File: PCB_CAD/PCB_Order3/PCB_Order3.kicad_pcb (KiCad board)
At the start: 4 copper layers, 88 parts, among them SW1 SLW-883935-2A-D

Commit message: pinned out 3 sides of the microcontroller
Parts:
- removed RCAA1, RCAA2: FW6190, CustomModels:FW6190
- removed RCAD1, RCAD2: RCJ-027, CustomModels:CUI_RCJ-027
- added J1: Conn_01x03_Socket, Connector_PinSocket_2.54mm:PinSocket_1x03_P2.54mm_Vertical_SMD_Pin1Right, F.Cu at (154.9, 137.9)
- added MbC1: 4.7u, Capacitor_SMD:C_0805_2012Metric_Pad1.18x1.45mm_HandSolder, F.Cu at (-25.4, 41.1)
- added PEC3: 47u, Capacitor_SMD:C_0805_2012Metric_Pad1.18x1.45mm_HandSolder, F.Cu at (-25.4, 44.1)
- added RCAAin1: FW6190, CustomModels:FW6190, F.Cu at (33.3, 145.5)
- added RCAAout1: FW6190, CustomModels:FW6190, F.Cu at (63.1, 145.5)
- added RCADin1: RCJ-027, CustomModels:CUI_RCJ-027, F.Cu at (97.0, 151.6)
- added RCADout1: RCJ-027, CustomModels:CUI_RCJ-027, F.Cu at (110.9, 151.5)
- MR1, MbC2, MbC3, MbC4, UR1, UR2: moved to B.Cu
- moved DCPEM1 160.2 mm to (199.5, 70.9), turned to 90 degrees
- moved DnC1 140.1 mm to (-68.5, 28.2)
- moved DrC1 140.1 mm to (-68.5, 31.2)
- moved FnC1 140.1 mm to (-68.5, 34.3)
- moved FnC2 140.1 mm to (-68.5, 37.3)
- moved LLSIC1 140.1 mm to (-68.5, 40.3)
- moved LLSIC2 140.1 mm to (-68.5, 43.3)
- moved LLSOC1 140.1 mm to (-68.5, 46.3)
- moved LLSOC2 140.1 mm to (-68.5, 49.3)
- moved LnC1 140.1 mm to (-68.5, 52.3)
- moved MnC1 140.1 mm to (-63.7, 37.3)
- moved MnC2 140.1 mm to (-63.7, 40.3)
- moved MnC3 140.1 mm to (-63.7, 43.3)
- moved MnC4 140.1 mm to (-63.7, 46.3)
- moved MnC5 140.1 mm to (-63.7, 49.3)
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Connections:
- DCPEM1 pad 1: Net-(DCPEM1-Pad1) -> GNDD
- DCPEM1 pad 2: Net-(DCPEM1-Pad2) -> VDD
- PEC1 pad 1: Net-(DCPEM1-Pad1) -> GNDD
- PEC1 pad 2: Net-(DCPEM1-Pad2) -> VDD
- PEC2 pad 1: Net-(DCPEM1-Pad1) -> GNDD
- PEC2 pad 2: Net-(DCPEM1-Pad2) -> VDD
- SPDIFTX1 pad 10: /I2S3_SDO -> /I2S2_SDO
- SPDIFTX1 pad 7: /I2S3_MCK -> /I2S2_MCK
- SPDIFTX1 pad 8: /I2S3_CK -> /I2S2_CK
- SPDIFTX1 pad 9: /I2S3_WS -> /I2S2_WS
- TVS1 pad 1: Net-(DCPEM1-Pad2) -> VDD
- TVS1 pad 2: Net-(DCPEM1-Pad1) -> GNDD
- uController1 pad 105: unconnected-(uController1-PA13-Pad105) -> /DEBUG_SWDIO
- uController1 pad 109: unconnected-(uController1-PA14-Pad109) -> /DEBUG_SWCLK
- uController1 pad 111: /I2S3_CK -> unconnected-(uController1-PC10-Pad111)
- uController1 pad 40: /I2S3_WS -> unconnected-(uController1-PA4-Pad40)
- uController1 pad 48: /I2S3_SDO -> unconnected-(uController1-PB2-Pad48)
- uController1 pad 97: /I2S3_MCK -> unconnected-(uController1-PC7-Pad97)
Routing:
- net /FMC_D0: track 0.00 -> 231.6 mm, vias 0 -> 6
- net /FMC_D7: track 0.00 -> 182.6 mm, vias 0 -> 6
- net /FMC_D6: track 0.00 -> 181.7 mm, vias 0 -> 6
- net /FMC_D5: track 0.00 -> 179.8 mm, vias 0 -> 6
- net /FMC_SDCLK: track 0.00 -> 151.8 mm, vias 0 -> 3
- net /FMC_D15: track 0.00 -> 141.6 mm, vias 0 -> 3
- net /FMC_D14: track 0.00 -> 137.0 mm, vias 0 -> 3
- net /FMC_BA1: track 0.00 -> 134.3 mm, vias 0 -> 3
- net /FMC_D13: track 0.00 -> 133.1 mm, vias 0 -> 3
- net /FMC_BA0: track 0.00 -> 133.0 mm, vias 0 -> 3
- net /I2S1_MCK: track 0.00 -> 123.9 mm, vias 0 -> 3
- net /I2S1_CK: track 0.00 -> 122.9 mm, vias 0 -> 3
- net /I2S1_SDI: track 0.00 -> 121.5 mm, vias 0 -> 3
- net /I2S2_WS: track 0.00 -> 107.9 mm, vias 0 -> 3
- net /I2S2_CK: track 0.00 -> 107.2 mm, vias 0 -> 3
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
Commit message: finished pinning out the microcontroller
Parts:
- moved SR1 195.5 mm to (122.7, 133.9), turned to 90 degrees
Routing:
- net /FMC_D3: track 0.00 -> 211.7 mm, vias 0 -> 6
- net /FMC_D2: track 0.00 -> 211.1 mm, vias 0 -> 6
- net /I2S1_WS: track 0.00 -> 116.6 mm, vias 0 -> 3
- net /FMC_NBL0: track 0.00 -> 99.9 mm, vias 0 -> 5
- net /FMC_SDNCAS: track 0.00 -> 88.9 mm, vias 0 -> 3
- net /FMC_NWE: track 0.00 -> 81.8 mm, vias 0 -> 3
- net /SPDIFRX_IN0: track 0.00 -> 80.1 mm, vias 0 -> 3
- net /FMC_NWAIT: track 0.00 -> 78.9 mm, vias 0 -> 3
- net /FMC_NBL1: track 0.00 -> 77.0 mm, vias 0 -> 3
- net /FMC_NOE: track 0.00 -> 74.7 mm, vias 0 -> 3
- net /DEBUG_SWCLK: track 0.00 -> 71.5 mm, vias 0 -> 1
- net /BOOTSW: track 0.00 -> 47.4 mm, vias 0 -> 1
- net /I2C1_SDA: track 0.00 -> 45.9 mm, vias 0 -> 1
- net /I2C1_SCL: track 0.00 -> 45.0 mm, vias 0 -> 1
- net VDD: track 14.5 -> 30.0 mm, vias 10 -> 20
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
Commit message: complete? pcb design
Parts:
- removed LLS1, LLS2: SN74AXCH1T45DCKR, CustomModels:DCK6_TEX
- added DXnC2: 0.1u, Capacitor_SMD:C_0805_2012Metric_Pad1.18x1.45mm_HandSolder, B.Cu at (109.1, 134.9)
- added DXnC3: 0.1u, Capacitor_SMD:C_0805_2012Metric_Pad1.18x1.45mm_HandSolder, B.Cu at (111.1, 134.9)
- added LLSIN1: SN74AXCH1T45DCKR, CustomModels:DCK6_TEX, F.Cu at (97.0, 143.1)
- added LLSOUT1: SN74AXCH1T45DCKR, CustomModels:DCK6_TEX, F.Cu at (110.8, 143.2)
- AB1, AbC1, AbC2, AdbC1, AdbC2, AnC1, AnC2, DB1, DacOut_L_decouple1, DacOut_L_res1, DacOut_R_decouple1, DacOut_R_res1, Dac_DigitalSup_noise1, Dac_DigitalSup_noise2, DbC1, DnC1, DrC1, FnC1, FnC2, PEC1, PEC2, PEC3, RnC1, RnC2, RnC3, RnC4, RnC5, RnC6, RnC7, SPDIFC1, SPDIFC2, SPDIFR1, SPDIFR2, VDIVR1, VDIVR2: moved to B.Cu
- DXnC1, LLSOC1: value 0.15u -> 0.1u; moved to B.Cu
- LLSOC2: value 0.15u -> 0.1u
- TVS1: footprint CustomModels:SOD-962 SL2_TOS -> Diode_SMD:D_0201_0603Metric_Pad0.64x0.40mm_HandSolder; moved to B.Cu
- moved PEC1 286.3 mm to (176.9, 122.1), turned to -90 degrees
- moved TVS1 284.4 mm to (178.3, 122.1), turned to 90 degrees
- moved PEC2 283.5 mm to (174.9, 122.1), turned to -90 degrees
- moved FnC1 252.3 mm to (177.3, 91.0), turned to 180 degrees
- moved FnC2 249.4 mm to (177.5, 78.0), turned to 180 degrees
- moved BC1 231.2 mm to (133.2, 132.1)
- moved DXnC1 213.3 mm to (113.1, 134.9), turned to -90 degrees
- moved PEC3 213.1 mm to (172.9, 122.1), turned to 90 degrees
- moved LLSOC1 206.3 mm to (113.5, 143.3), turned to 180 degrees
- moved LLSOC2 199.8 mm to (107.5, 143.6), turned to 90 degrees
- moved LnC1 196.7 mm to (128.2, 53.4)
- moved MnC6 195.4 mm to (127.7, 91.7), turned to 90 degrees
- moved LLSIC2 195.3 mm to (101.0, 140.3), turned to 90 degrees
- moved MnC2 195.3 mm to (127.5, 80.0), turned to 90 degrees
- moved MnC4 195.2 mm to (127.5, 85.2), turned to 90 degrees
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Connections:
- SPDIFTX1 pad 36: unconnected-(SPDIFTX1-VDDRX-Pad36) -> VDD
- SPDIFTX1 pad 38: unconnected-(SPDIFTX1-GNDRX-Pad38) -> GNDD
- SPDIFTX1 pad 41: unconnected-(SPDIFTX1-AGND-Pad41) -> GNDD
- SPDIFTX1 pad 42: unconnected-(SPDIFTX1-VCC-Pad42) -> VDD
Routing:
- net GNDD: track 32.1 -> 154.1 mm, vias 16 -> 65
- net VDD: track 30.0 -> 128.7 mm, vias 20 -> 51
- net /I2S2_SDO: track 0.00 -> 91.8 mm, vias 0 -> 3
- net /I2C2_SDA: track 64.8 -> 25.1 mm
- net /I2C2_SCL: track 61.9 -> 23.8 mm
- net /KP_Col3: track 84.0 -> 47.5 mm
- net /KP_Row2: track 85.9 -> 49.6 mm
- net /KP_Row1: track 83.4 -> 47.4 mm
- net /KP_Row3: track 87.4 -> 51.5 mm
- net /KP_Col2: track 89.0 -> 53.3 mm
- net /KP_Col1: track 90.7 -> 55.4 mm
- net /KP_Row4: track 72.6 -> 37.6 mm
- net /KP_Col5: track 78.7 -> 44.2 mm
- net /KP_Col4: track 79.2 -> 44.9 mm
- net /I2S2_MCK: track 91.8 -> 115.1 mm, vias 3 -> 5
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
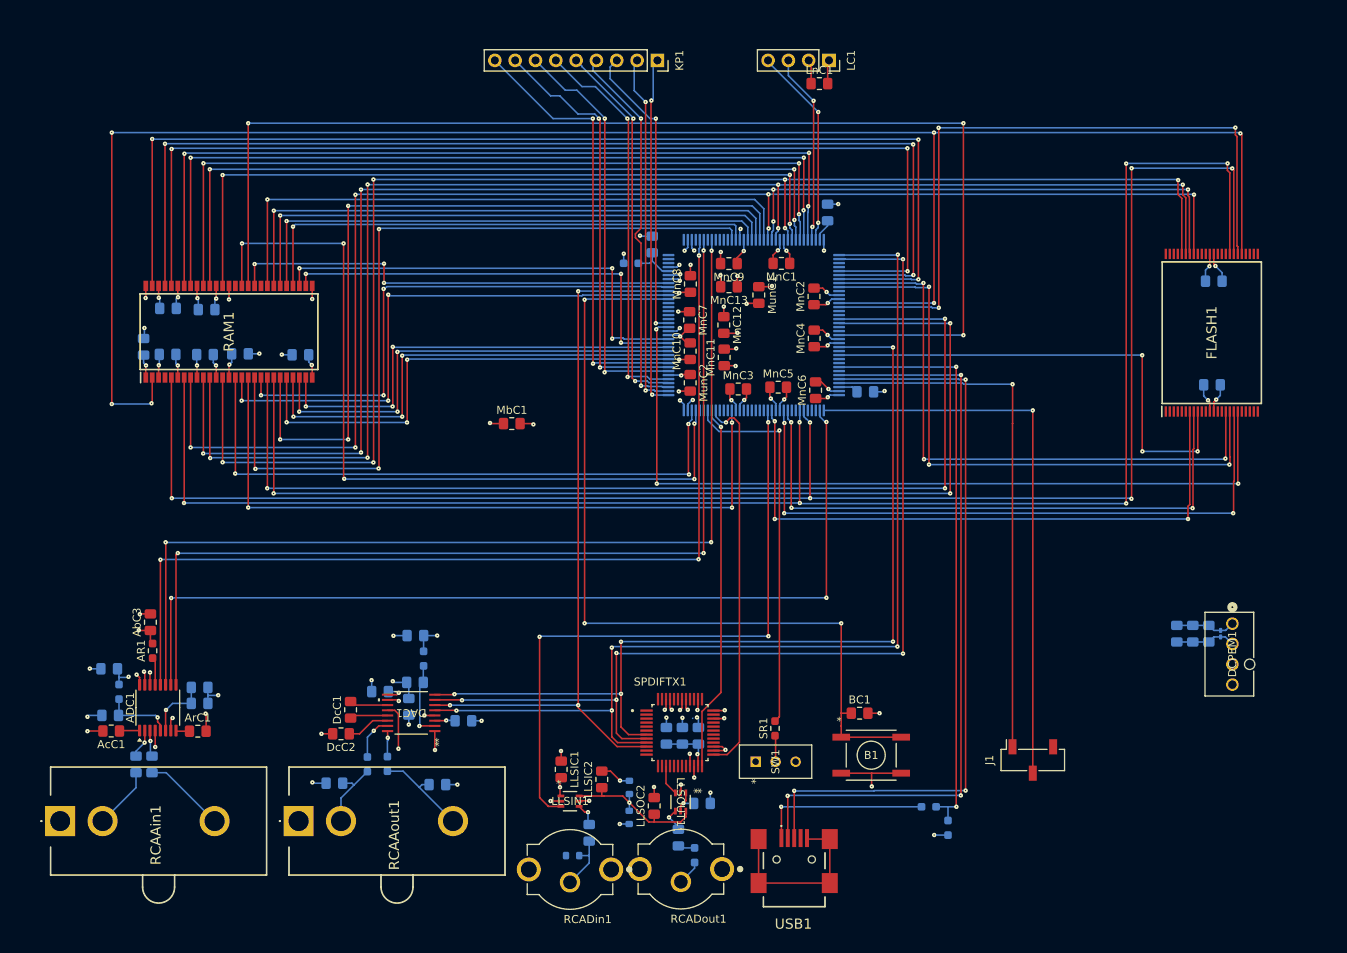
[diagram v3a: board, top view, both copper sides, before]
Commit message: cleaned up silkscreen and added ground planes
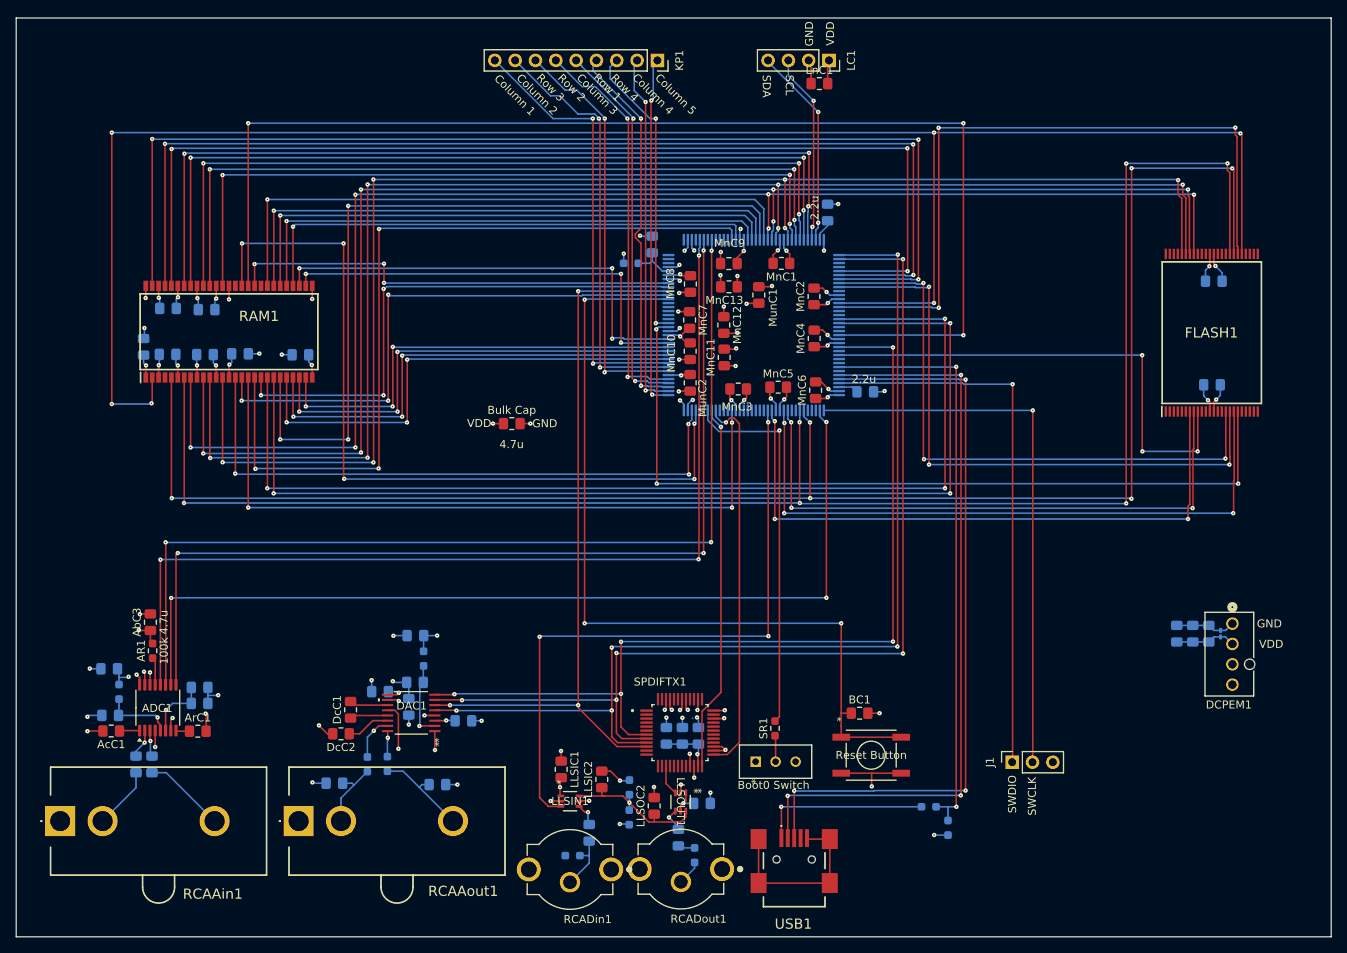
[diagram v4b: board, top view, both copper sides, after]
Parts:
- Boot0 Switch: renamed from SW1
- Bulk Cap: renamed from MbC1
- DbC1: value 15u -> 10u
- DnC1, FnC1, FnC2, LLSIC1, LLSIC2, LnC1, RnC1, RnC2, RnC3, RnC4, RnC5, RnC6, RnC7: value 0.15u -> 0.1u
- DsnC1: renamed from Dac_DigitalSup_noise1; value 0.15u -> 0.1u
- DsnC1: renamed from Dac_DigitalSup_noise2; value 0.15u -> 0.1u
- J1: footprint Connector_PinSocket_2.54mm:PinSocket_1x03_P2.54mm_Vertical_SMD_Pin1Right -> Connector_PinSocket_2.54mm:PinSocket_1x03_P2.54mm_Vertical
- Reset Button: renamed from B1
- SPDIFR1, VDIVR1, VDIVR2: footprint Resistor_SMD:R_0603_1608Metric -> Resistor_SMD:R_0603_1608Metric_Pad0.98x0.95mm_HandSolder
- moved J1 2.59 mm to (152.3, 138.2)
- renumbered DacOut_L_decouple1 to DacOutLCap, DacOut_L_res1 to DacOutLRes, DacOut_R_decouple1 to DacOutRCap, DacOut_R_res1 to DacOutRRes
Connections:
- uController1 pad 31: GNDA -> GNDD
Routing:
- net /DEBUG_SWDIO: track 67.1 -> 69.0 mm
- net GNDD: track 154.1 -> 155.9 mm
- net GNDA: track 11.9 -> 10.4 mm, vias 4 -> 3
- net /DEBUG_SWCLK: track 71.5 -> 70.1 mm
- added copper zone on In2.Cu, net GNDA
- added copper zone on In2.Cu, net GNDD
- added copper zone on In1.Cu, net VDD
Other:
- board outline added: 164.4 x 114.8 mm
- board text added: "2.2u"
- board text added: "Column 1"
- board text added: "Column 2"
- board text added: "Column 3"
- board text added: "Column 4"
- board text added: "Column 5"
- board text added: "GND"
- board text added: "Row 1"
- board text added: "Row 2"
- board text added: "Row 3"
- board text added: "Row 4"
- board text added: "SCL"
- board text added: "SDA"
- board text added: "SWCLK"
- board text added: "SWDIO"
- board text added: "VDD"
